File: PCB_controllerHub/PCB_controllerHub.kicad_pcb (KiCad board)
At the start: 2 copper layers, 123 x 80 mm, 15 parts, among them J1 Screw_Terminal_01x02, J2 Screw_Terminal_01x02, Q1 TIP42, T1 Transformer_1P_SS, U1 Module_Relay

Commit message: [PCB Medidores e Correção]
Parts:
- moved C3 5.08 mm to (188.0, 64.8)
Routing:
- net +5V: track 103.7 -> 101.6 mm
- net (no net): vias 4 -> 8

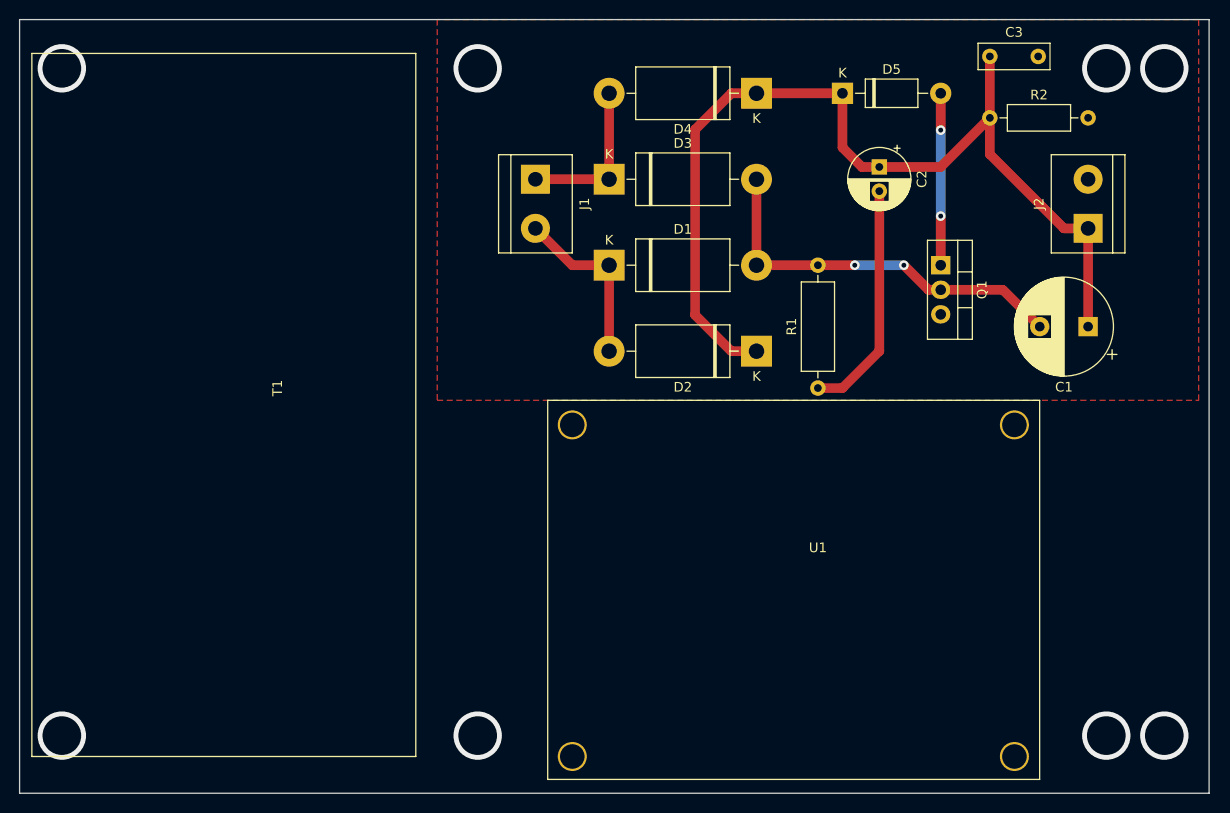
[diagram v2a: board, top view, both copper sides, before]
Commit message: Fix minor error in ControllerHub Power Supply & Git files cleanup
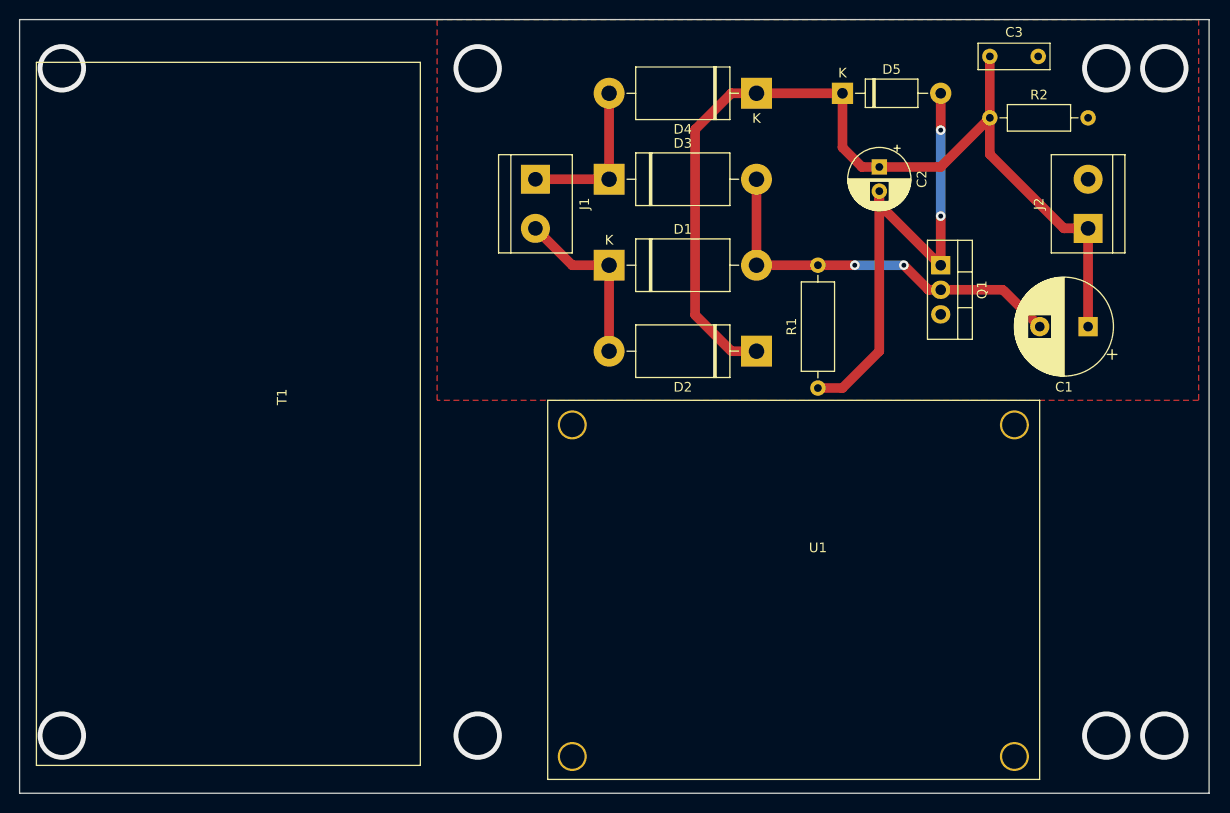
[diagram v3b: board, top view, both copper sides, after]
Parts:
- moved T1 1.03 mm to (89.4, 138.1)
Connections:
- D5 pad 2: Net-(D5-Pad2) -> Net-(C2-Pad2)
- Q1 pad 1: Net-(D5-Pad2) -> Net-(C2-Pad2)
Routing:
- net Net-(C2-Pad2): track 24.5 -> 52.6 mm, vias 0 -> 2
- net Net-(D5-Pad2): track 17.8 -> 0.00 mm, vias 2 -> 0
